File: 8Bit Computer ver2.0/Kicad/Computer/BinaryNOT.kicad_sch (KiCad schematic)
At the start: 4 parts, among them IC13 SN74LVC1G14DBVR, IC14 SN74LVC1G14DBVR, IC15 SN74HCS74DR, IC16 SN74ABT821ADWR

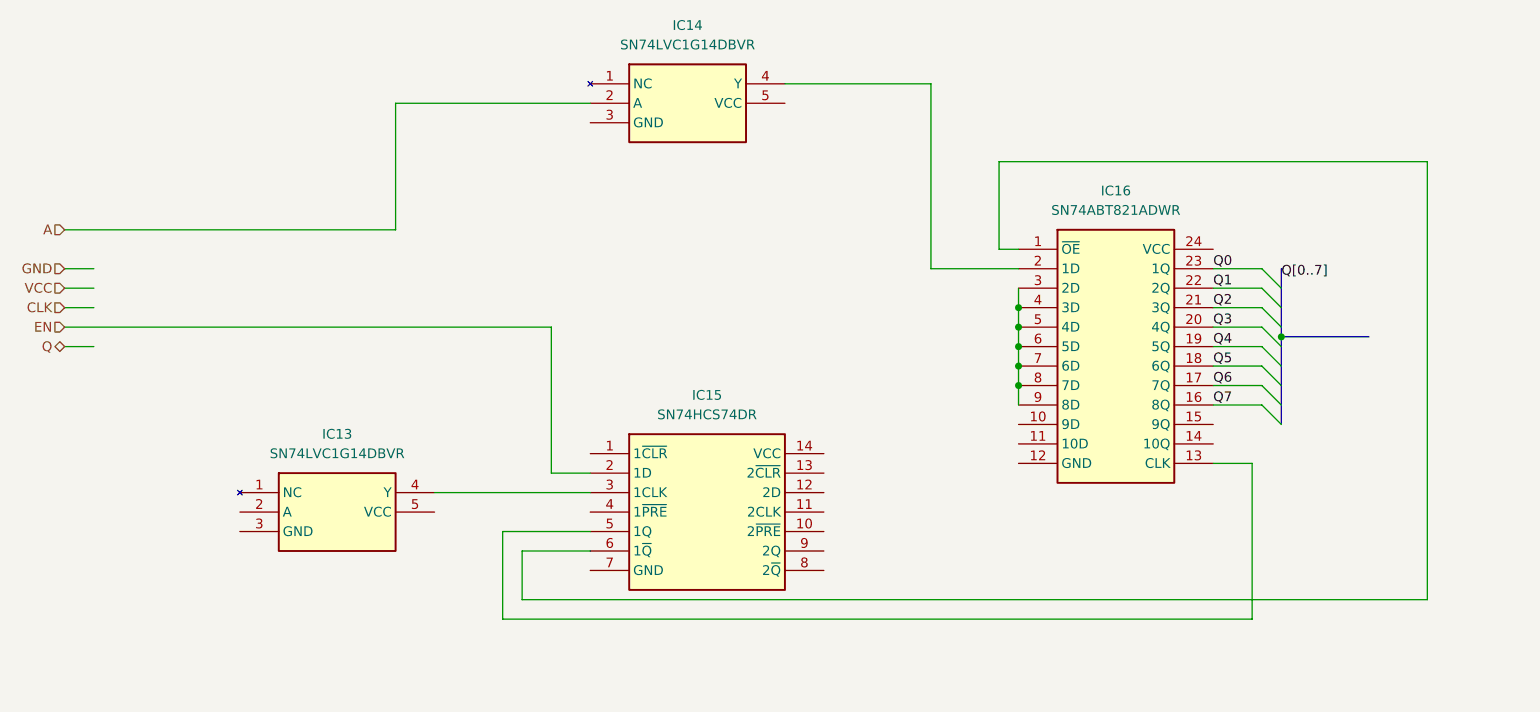
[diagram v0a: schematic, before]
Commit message: parts,Kicad
added 74HCS574 to Kicad
Kicad:
ALU->added Bitwise NOT,OR,XOR,AND
ALU->added A,B 8in OR
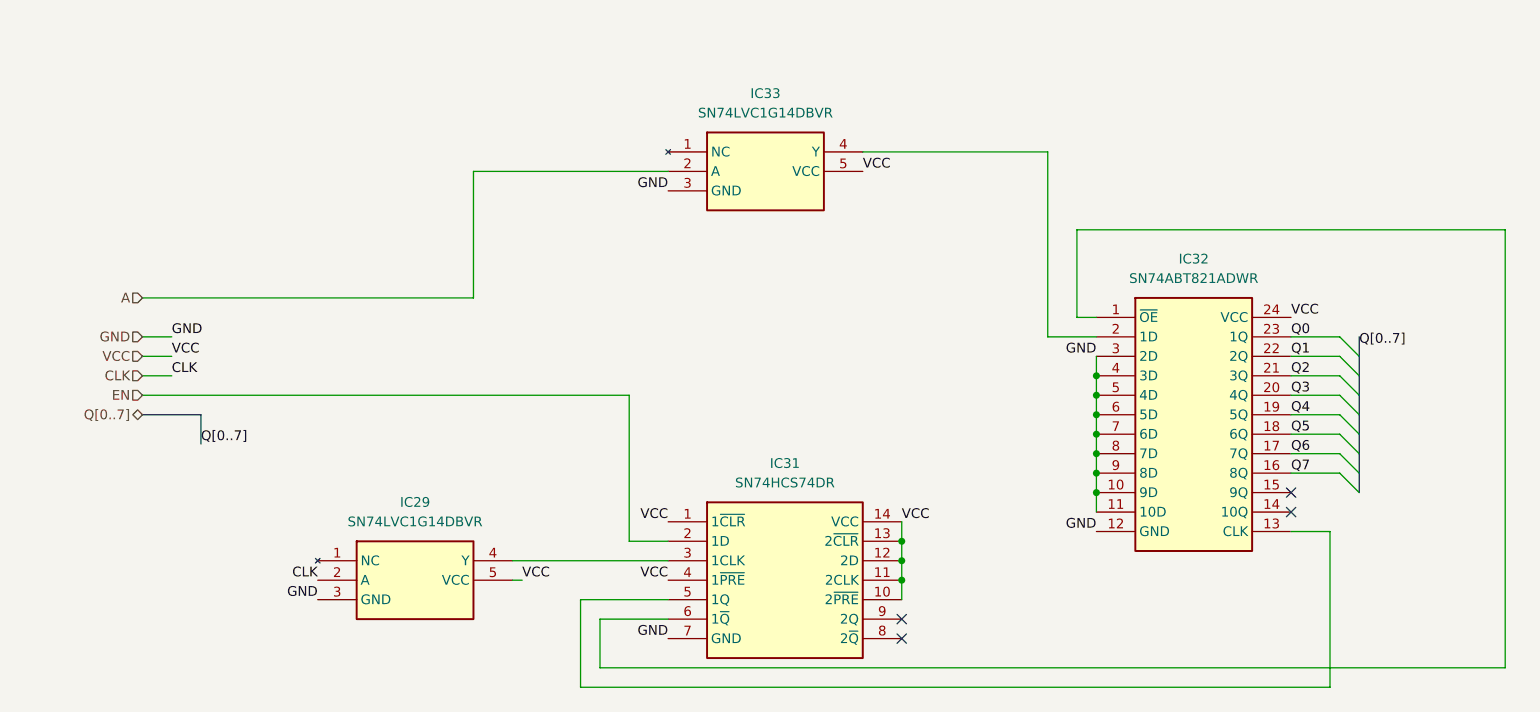
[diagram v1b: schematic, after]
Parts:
- removed IC13, IC14: SN74LVC1G14DBVR, Samacsys:SOT95P280X145-5N, symbol Samacsys:SN74LVC1G14DBVR
- removed IC15: SN74HCS74DR, Samacsys:SOIC127P600X175-14N, symbol Samacsys:SN74HCS74DR
- removed IC16: SN74ABT821ADWR, Samacsys:SOIC127P1030X265-24N, symbol Samacsys:SN74ABT821ADWR
- added IC29, IC33: SN74LVC1G14DBVR, Samacsys:SOT95P280X145-5N, symbol Samacsys:SN74LVC1G14DBVR
- added IC31: SN74HCS74DR, Samacsys:SOIC127P600X175-14N, symbol Samacsys:SN74HCS74DR
- added IC32: SN74ABT821ADWR, Samacsys:SOIC127P1030X265-24N, symbol Samacsys:SN74ABT821ADWR
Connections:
- net A: now also IC33.2 (A)
- net CLK: now also IC29.2 (A)
- net EN: now also IC31.2 (1D)
- net GND: now also IC29.3 (GND), IC31.7 (GND), IC32.10 (9D), IC32.11 (10D), IC32.12 (GND), IC32.3 (2D), IC32.4 (3D), IC32.5 (4D), IC32.6 (5D), IC32.7 (6D), IC32.8 (7D), IC32.9 (8D), IC33.3 (GND)
- net Q0: now also IC32.23 (1Q)
- net Q1: now also IC32.22 (2Q)
- net Q2: now also IC32.21 (3Q)
- net Q3: now also IC32.20 (4Q)
- net Q4: now also IC32.19 (5Q)
- net Q5: now also IC32.18 (6Q)
- net Q6: now also IC32.17 (7Q)
- net Q7: now also IC32.16 (8Q)
- net VCC: now also IC29.5 (VCC), IC31.1 (1~{CLR}), IC31.10 (2~{PRE}), IC31.11 (2CLK), IC31.12 (2D), IC31.13 (2~{CLR}), IC31.14 (VCC), IC31.4 (1~{PRE}), IC32.24 (VCC), IC33.5 (VCC)
- new net: IC31.6 (1~{Q}), IC32.1 (~{OE})
- new net: IC31.5 (1Q), IC32.13 (CLK)
- new net: IC32.2 (1D), IC33.4 (Y)
- new net: IC29.4 (Y), IC31.3 (1CLK)
- no-connect marks 0 -> 4

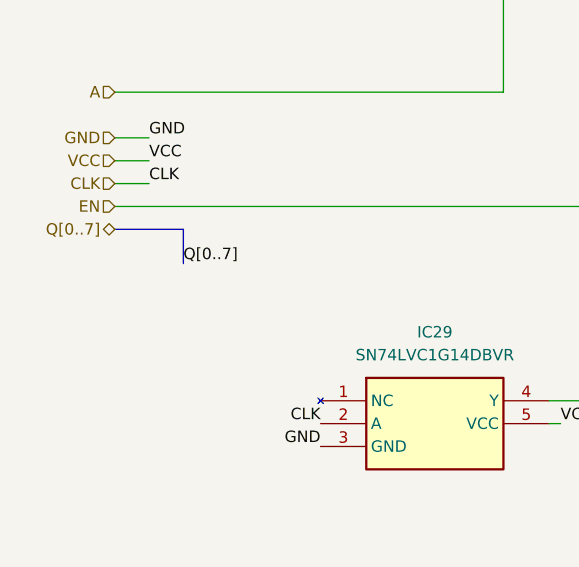
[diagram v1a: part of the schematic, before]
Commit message: Kicad,parts
Kicad:
added FlagRegister
began Inc, Comp
parts:
added comparator for P>Q 682
added faster sram 12ns AS7C
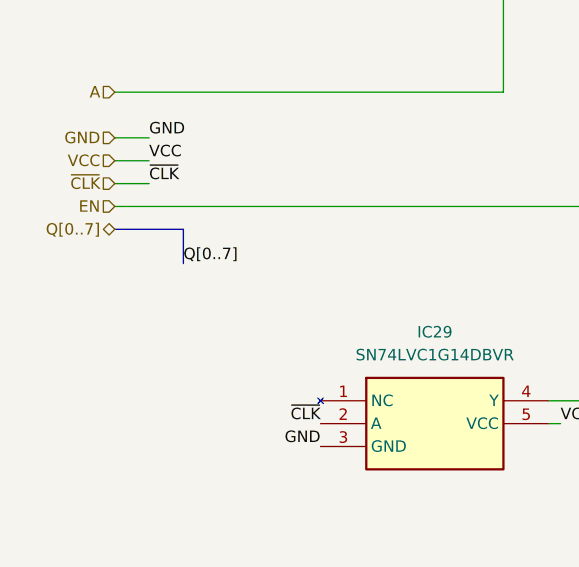
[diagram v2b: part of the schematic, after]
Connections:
- net CLK renamed ~{CLK}
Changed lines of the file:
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@@
 		)
 	)
-	(label "CLK"
+	(label "~{CLK}"
 		(at 59.69 91.44 0)
 		(effects
@@
 		)
 	)
-	(label "CLK"
+	(label "~{CLK}"
 		(at 78.74 118.11 180)
 		(effects
@@
 		)
 	)
-	(hierarchical_label "CLK"
+	(hierarchical_label "~{CLK}"
 		(shape input)
 		(at 55.88 91.44 180)

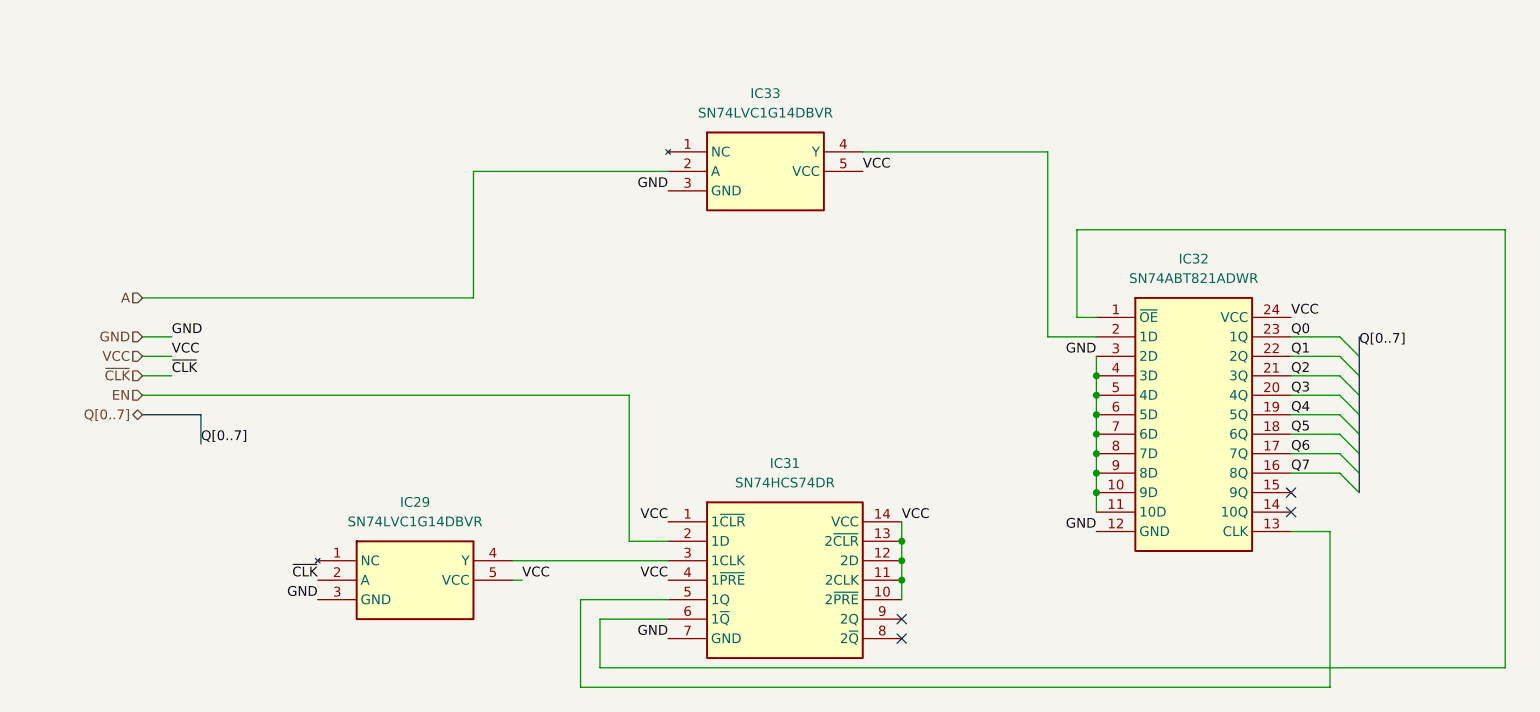
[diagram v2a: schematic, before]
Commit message: parts,Kicad
parts:
changed 8xDlatch HCS to ABT 574
waiting for SRAM CAD Model
Kicad:
imported AHC types of ICs
added ProgrammeCounter
finished Comparator
changed all HCS to AHC except 3in OR ->no AHC Version
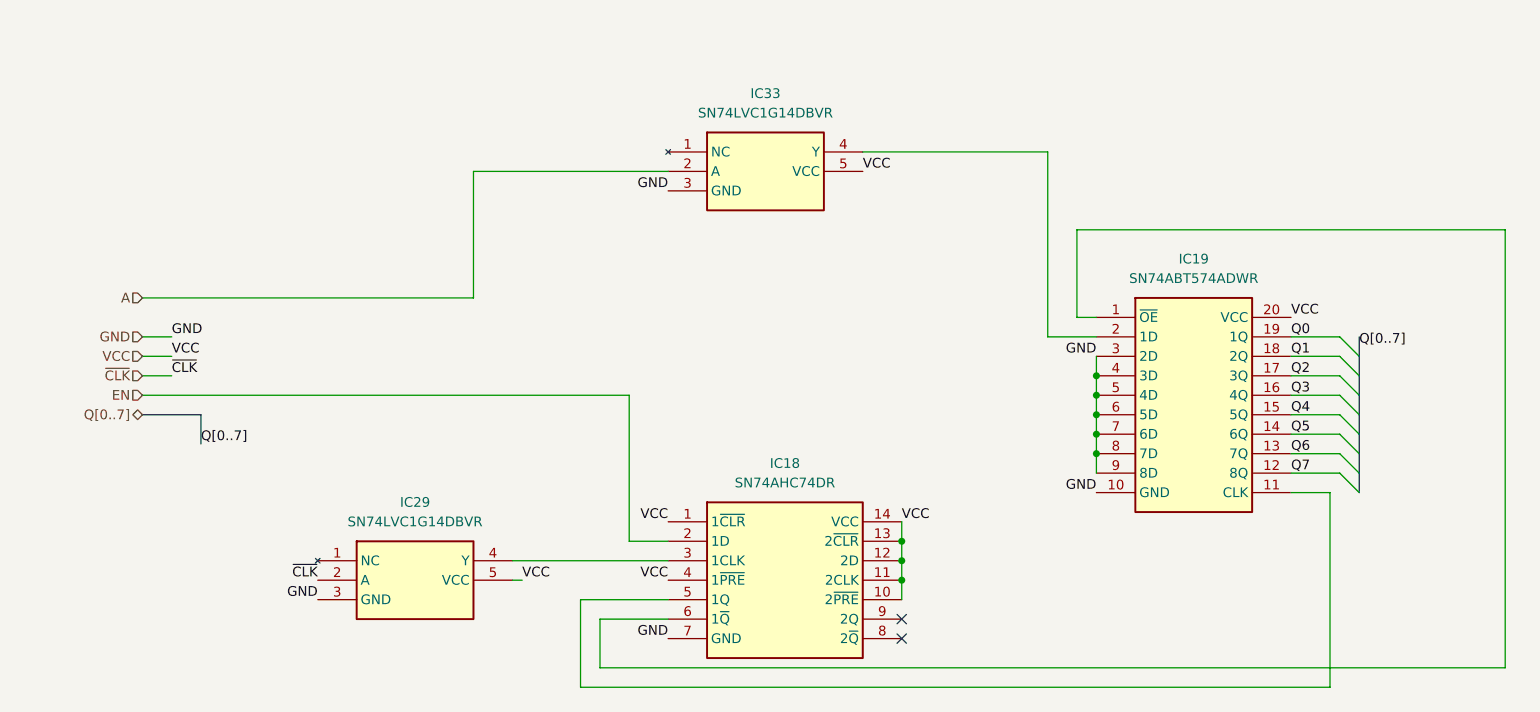
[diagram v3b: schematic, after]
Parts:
- removed IC31: SN74HCS74DR, Samacsys:SOIC127P600X175-14N, symbol Samacsys:SN74HCS74DR
- removed IC32: SN74ABT821ADWR, Samacsys:SOIC127P1030X265-24N, symbol Samacsys:SN74ABT821ADWR
- added IC18: SN74AHC74DR, Samacsys:SOIC127P600X175-14N, symbol Samacsys:SN74AHC74DR
- added IC19: SN74ABT574ADWR, Samacsys:SOIC127P1030X265-20N, symbol Samacsys:SN74ABT574ADWR
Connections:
- net EN: now also IC18.2 (1D)
- net GND: now also IC18.7 (GND), IC19.10 (GND), IC19.3 (2D), IC19.4 (3D), IC19.5 (4D), IC19.6 (5D), IC19.7 (6D), IC19.8 (7D), IC19.9 (8D)
- net Q0: now also IC19.19 (1Q)
- net Q1: now also IC19.18 (2Q)
- net Q2: now also IC19.17 (3Q)
- net Q3: now also IC19.16 (4Q)
- net Q4: now also IC19.15 (5Q)
- net Q5: now also IC19.14 (6Q)
- net Q6: now also IC19.13 (7Q)
- net Q7: now also IC19.12 (8Q)
- net VCC: now also IC18.1 (1~{CLR}), IC18.10 (2~{PRE}), IC18.11 (2CLK), IC18.12 (2D), IC18.13 (2~{CLR}), IC18.14 (VCC), IC18.4 (1~{PRE}), IC19.20 (VCC)
- net at IC33.4 (Y): now also IC19.2 (1D)
- net at IC29.4 (Y): now also IC18.3 (1CLK)
- new net: IC18.5 (1Q), IC19.11 (CLK)
- new net: IC18.6 (1~{Q}), IC19.1 (~{OE})
- no-connect marks 4 -> 2

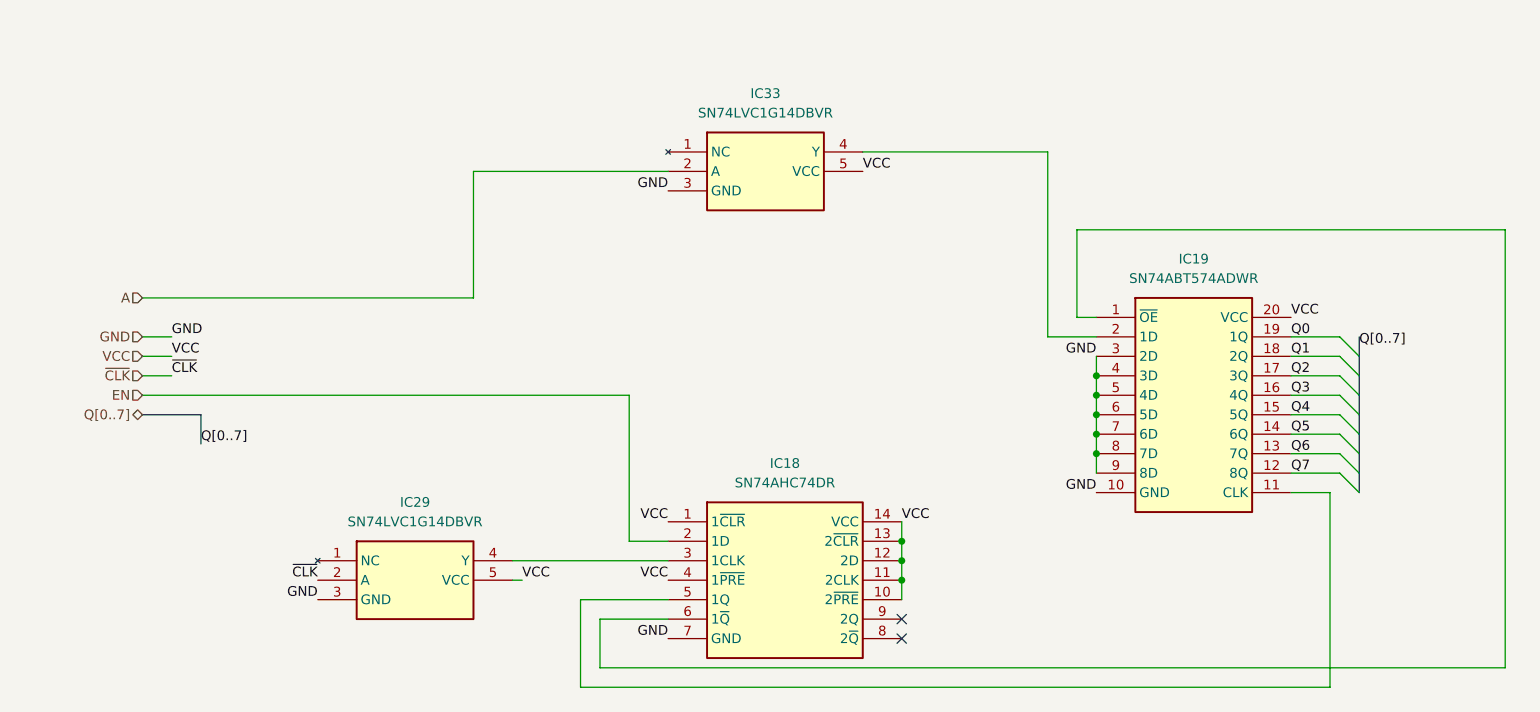
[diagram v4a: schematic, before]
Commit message: Kicad, parts
Parts:
added Leds
Kicad:
added Input Output
changed Q bus to DAT bus
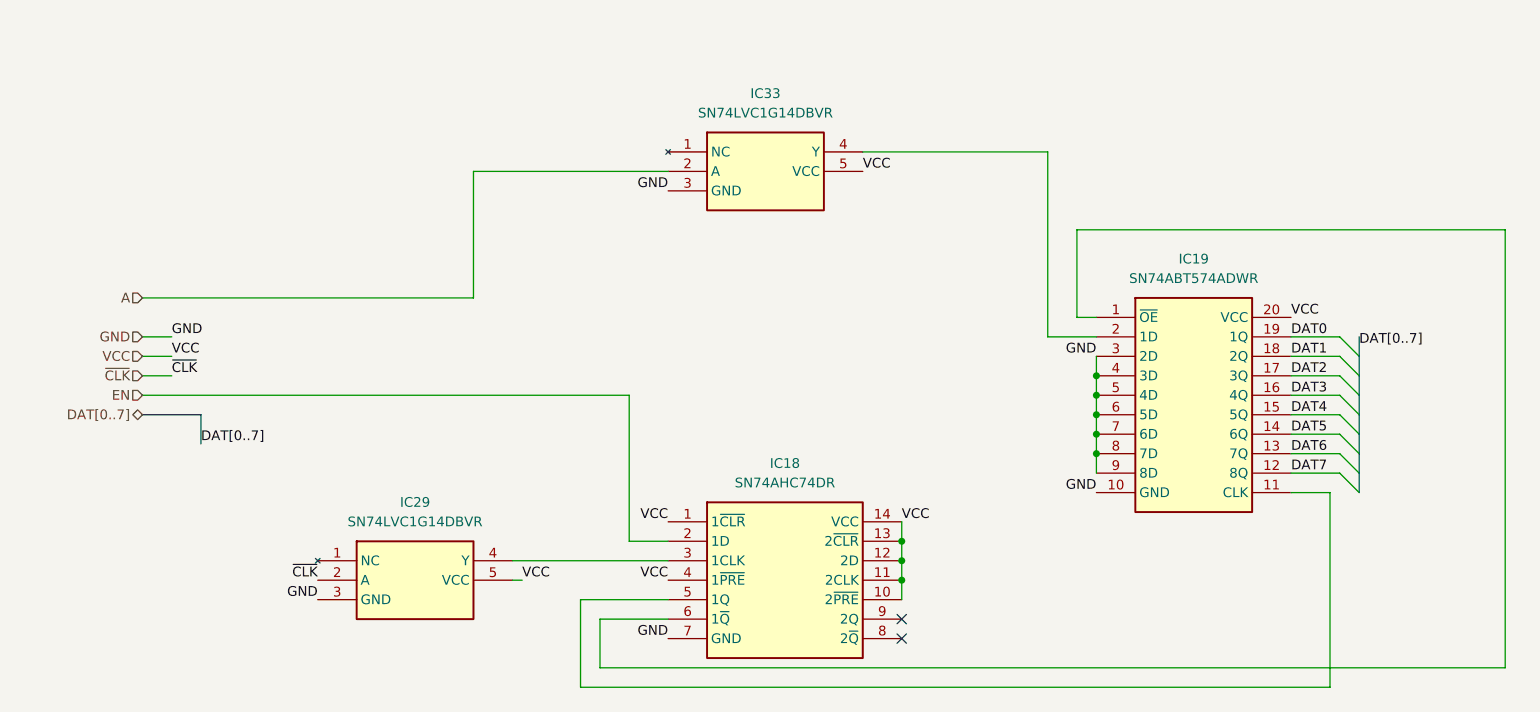
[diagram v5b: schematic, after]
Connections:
- net Q0 renamed DAT0
- net Q1 renamed DAT1
- net Q2 renamed DAT2
- net Q3 renamed DAT3
- net Q4 renamed DAT4
- net Q5 renamed DAT5
- net Q6 renamed DAT6
- net Q7 renamed DAT7
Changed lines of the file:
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@@
 		)
 	)
-	(label "Q2"
+	(label "DAT2"
 		(at 205.74 91.44 0)
 		(effects
@@
 		)
 	)
-	(label "Q[0..7]"
+	(label "DAT[0..7]"
 		(at 214.63 87.63 0)
 		(effects
@@
 		)
 	)
-	(label "Q0"
+	(label "DAT0"
 		(at 205.74 86.36 0)
 		(effects
@@
 		)
 	)
-	(label "Q6"
+	(label "DAT6"
 		(at 205.74 101.6 0)
 		(effects
@@
 		)
 	)
-	(label "Q7"
+	(label "DAT7"
 		(at 205.74 104.14 0)
 		(effects
@@
 		)
 	)
-	(label "Q[0..7]"
+	(label "DAT[0..7]"
 		(at 63.5 100.33 0)
 		(effects
@@
 		)
 	)
-	(label "Q4"
+	(label "DAT4"
 		(at 205.74 96.52 0)
 		(effects
@@
 		)
 	)
-	(label "Q5"
+	(label "DAT5"
 		(at 205.74 99.06 0)
 		(effects
@@
 		)
 	)
-	(label "Q3"
+	(label "DAT3"
 		(at 205.74 93.98 0)
 		(effects
@@
 		)
 	)
-	(label "Q1"
+	(label "DAT1"
 		(at 205.74 88.9 0)
 		(effects
@@
 		)
 	)
-	(hierarchical_label "Q[0..7]"
+	(hierarchical_label "DAT[0..7]"
 		(shape tri_state)
 		(at 55.88 96.52 180)

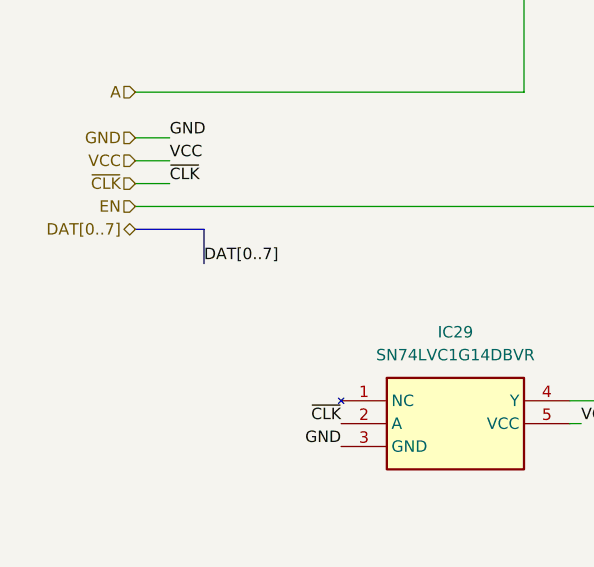
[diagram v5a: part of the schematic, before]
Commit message: Kicad, parts
parts:
added USB C PD Triggerboard
added Delay Chip for 90ns
added Push Button
Kicad:
added USB C PD Triggerboard
added rising edge detector via Delay and Xor for Accept Push Button
added VBUS net
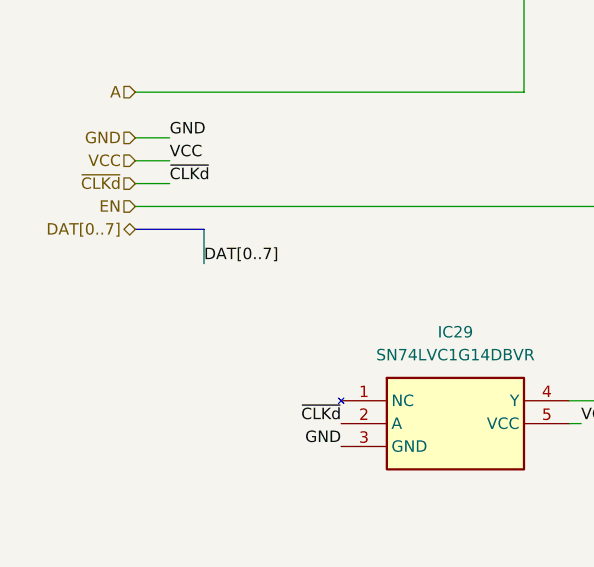
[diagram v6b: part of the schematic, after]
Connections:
- net ~{CLK} renamed ~{CLKd}
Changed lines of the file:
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@@
 		)
 	)
-	(label "~{CLK}"
+	(label "~{CLKd}"
 		(at 59.69 91.44 0)
 		(effects
@@
 		)
 	)
-	(label "~{CLK}"
+	(label "~{CLKd}"
 		(at 78.74 118.11 180)
 		(effects
@@
 		)
 	)
-	(hierarchical_label "~{CLK}"
+	(hierarchical_label "~{CLKd}"
 		(shape input)
 		(at 55.88 91.44 180)
